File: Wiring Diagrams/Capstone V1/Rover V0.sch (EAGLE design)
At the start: 65 parts, among them J8 DNP, J9 DNP, Q1 BSS138, Q2 BSS138, U1 MIC5225-3.3, U2 CJT1117-3.3, U3 SN74LVC1G125DCKR, U4 ARDUINOR3-BPLACE, Y1 32.768kHz

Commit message: Added raspberry pi to wiring diagrams
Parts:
- removed S2: BUTTON-CONDUCTIVESMD, SparkFun-Switches:BUTTON-CONDUCTIVESMD
- added FRAME4: FRAME-LETTER, SparkFun-Aesthetics:FRAME-LETTER
- added J1: RASPBERRYPI-40-PIN-GPIO_PTH_NO_SHROUD, SparkFun-Connectors:RASPBERRYPI-40-PIN-GPIO_PTH_NO_SHROUD
- added M1: SERVO, SparkFun-Electromechanical:SERVO
- added R17: 1.6k, SparkFun-Resistors:1.6KOHM-0603-1/10W-1%
- added R18: 3.3k, SparkFun-Resistors:3.3KOHM-0603-1/10W-1%
- added S1: DIP-04SMD, SparkFun-Switches:DIP-04SMD
- added S3, S4: (no value), switch:M9040P
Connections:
- new net ARD_RX: S1.1A, U4.D0
- new net ARD_TX: S1.2A, U4.D1
- new net N$18: R17.2, S1.2B
- new net N$19: BT8.+, C1.1, S4.S
- new net N$21: C2.1, S3.O, U$1.5V
- new net RPI_RX: J1.RXI, R17.1, R18.2
- new net RPI_TX: J1.TXO, S1.1B
- new net SERVO_PWM: M1.SIG, U4.D11
- net 12V: now also S4.P; no longer BT8.+, C1.1
- net 5V: now also J1.5V, M1.V+, S3.P; no longer C2.1, U$1.5V
- net GND: now also J1.GND, M1.GND, R18.1, S1.3B, S3.S, S4.O; no longer S2.2
- net RST: now also S1.3A; no longer S2.1

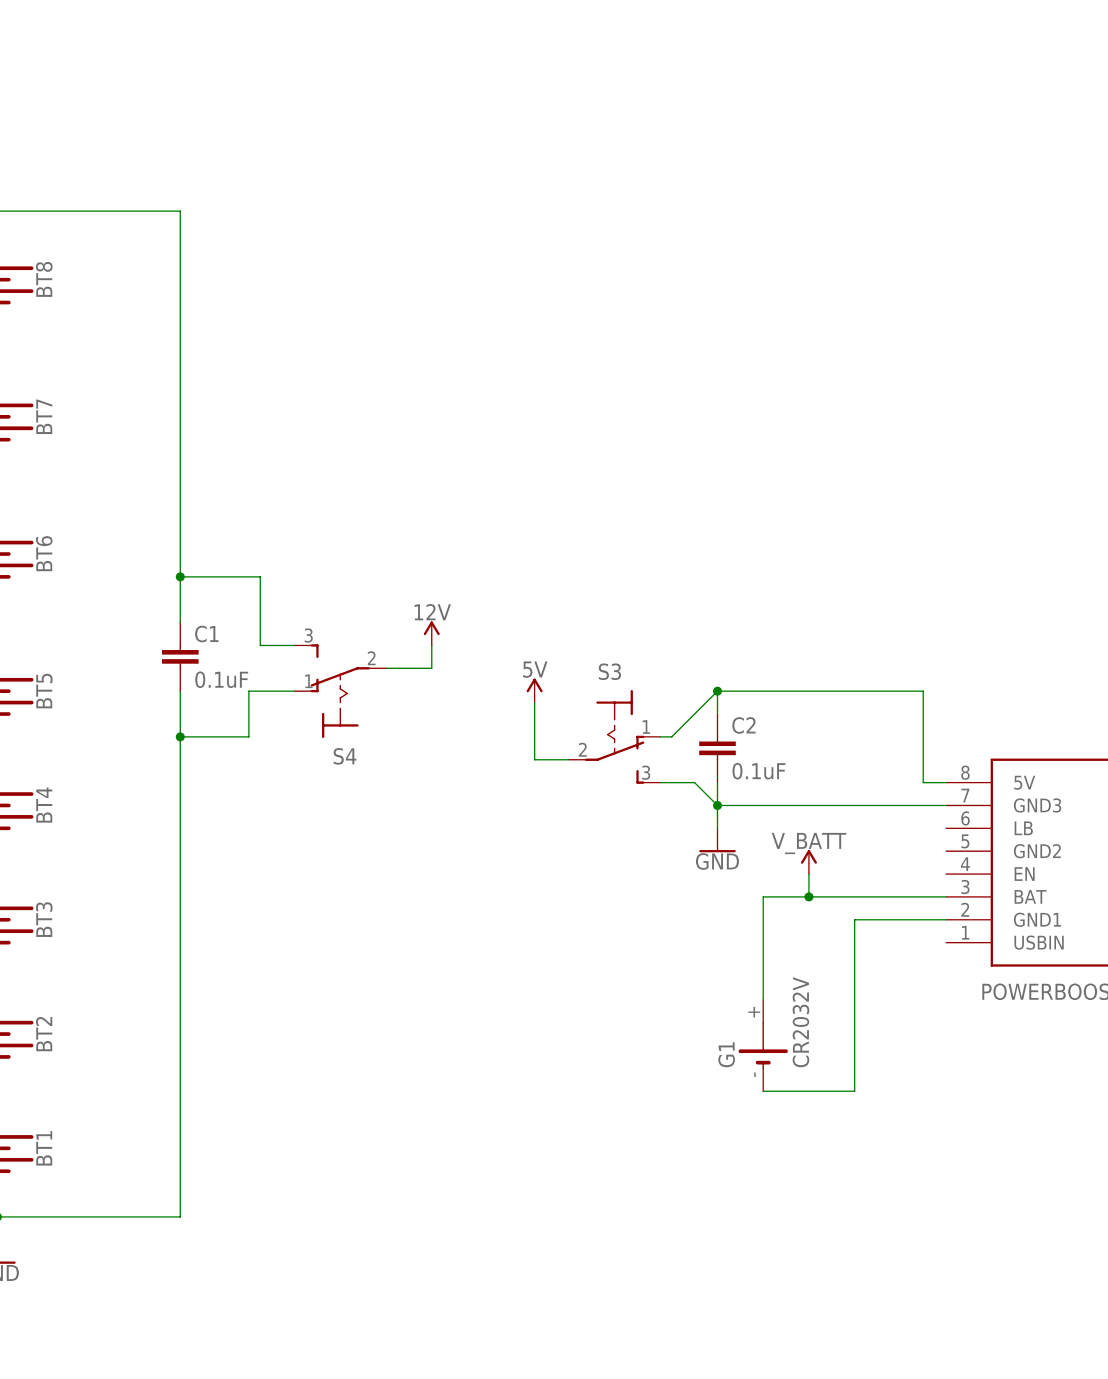
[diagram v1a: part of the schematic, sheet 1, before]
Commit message: Added encoders to wiring diagram rover and saved to pdf
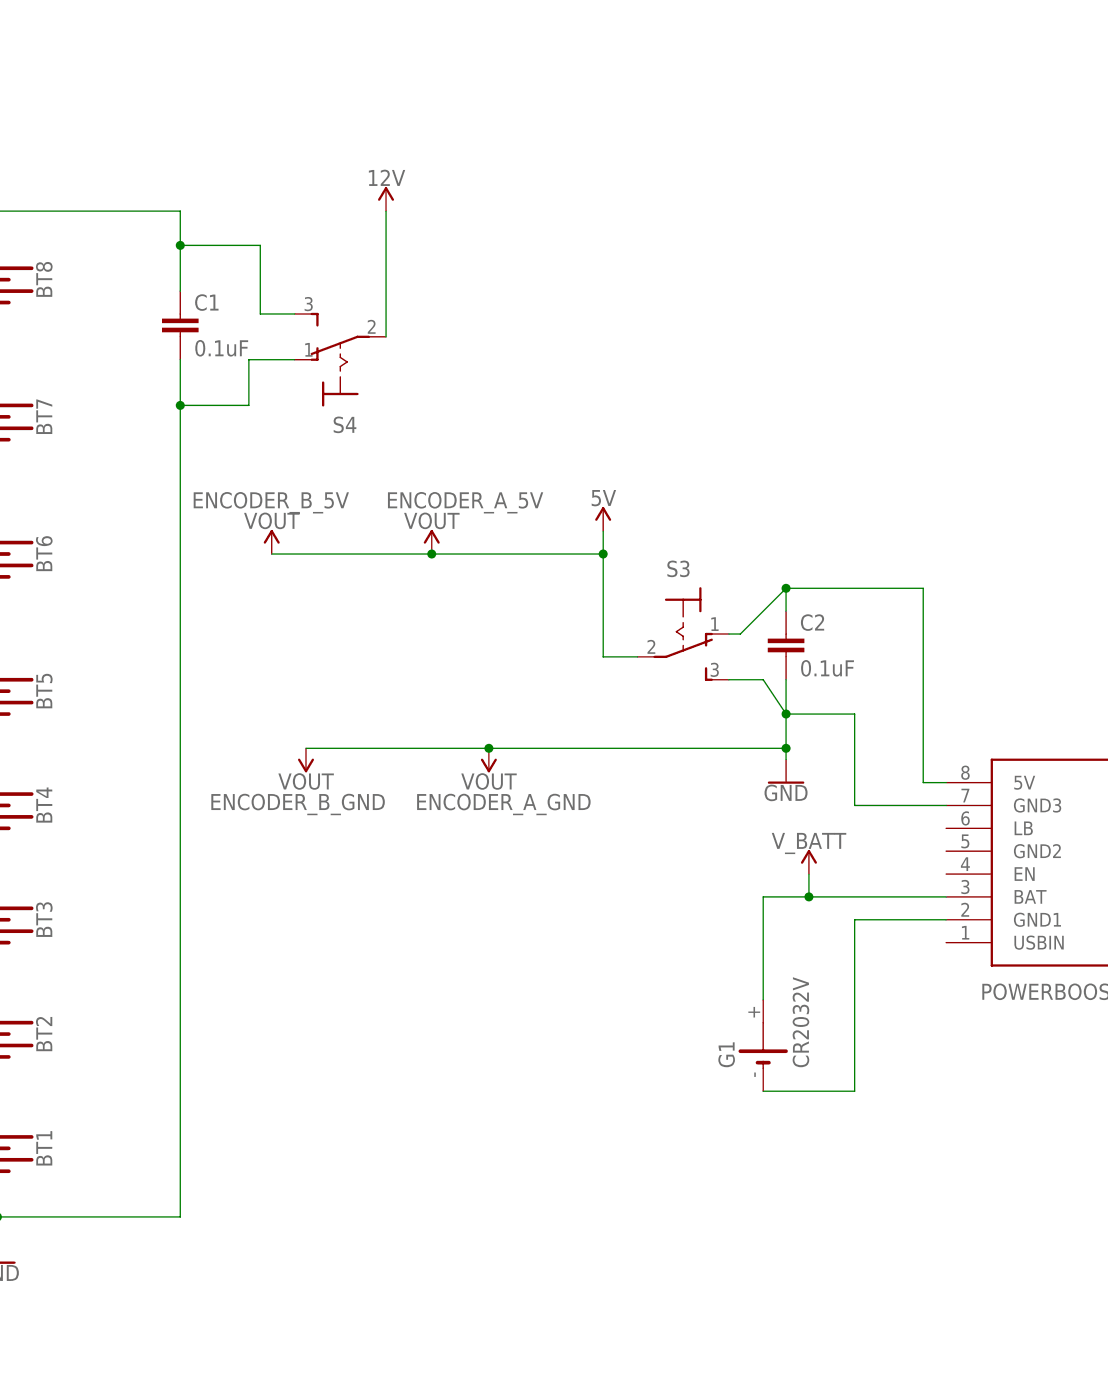
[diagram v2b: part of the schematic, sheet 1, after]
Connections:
- new net ENCODER_A_IN: U4.D8
- new net ENCODER_B_IN: U4.D9
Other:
- moved on the sheet: C1, C2, S3, S4
